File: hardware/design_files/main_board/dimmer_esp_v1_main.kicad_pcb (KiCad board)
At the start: 2 copper layers, 44 x 49.5 mm, 53 parts, among them IC1 PEC11S-929K-S0015, J1 SM05B-SRSS-TB_LF__SN_, J4 Conn_01x02, J5 Conn_01x02, J6 Conn_01x02, J7 Conn_01x04, J8 Screw_Terminal_01x03, K1 FTR-LYCA005Y, SW1 Commission, SW2 Reset, SW3 Toggle, U1 74AHC1G14, U2 LDO: SPX3819M5-L-3-3, U3 ESP32-C6-MINI, U4 SN74LV1T125DBVR, U6 SN74LVC1G74DCUR

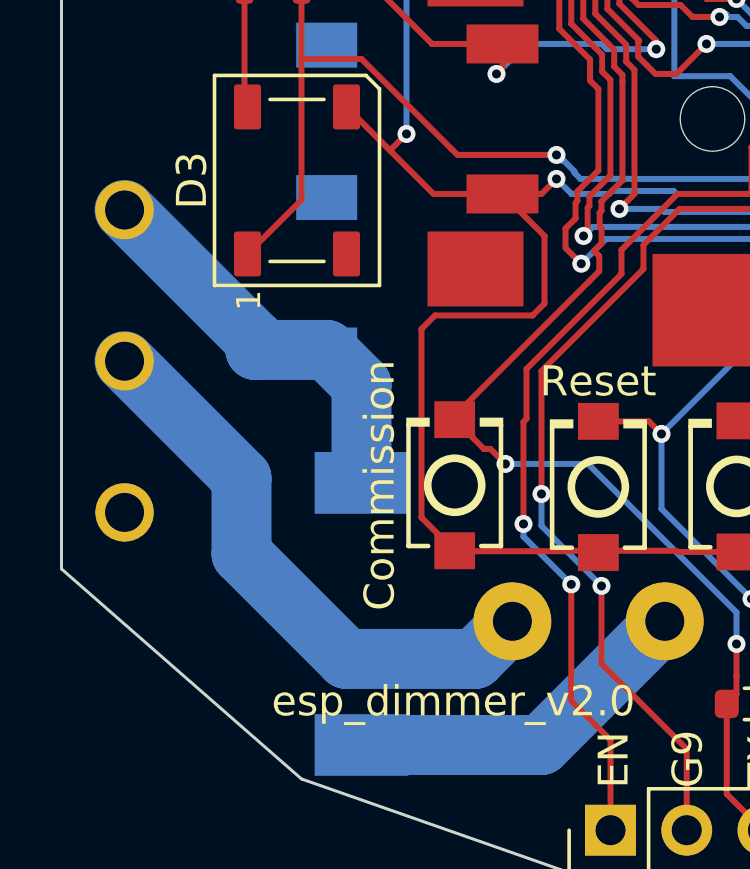
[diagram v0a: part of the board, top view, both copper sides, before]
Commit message: Fix trace before remove debug interface
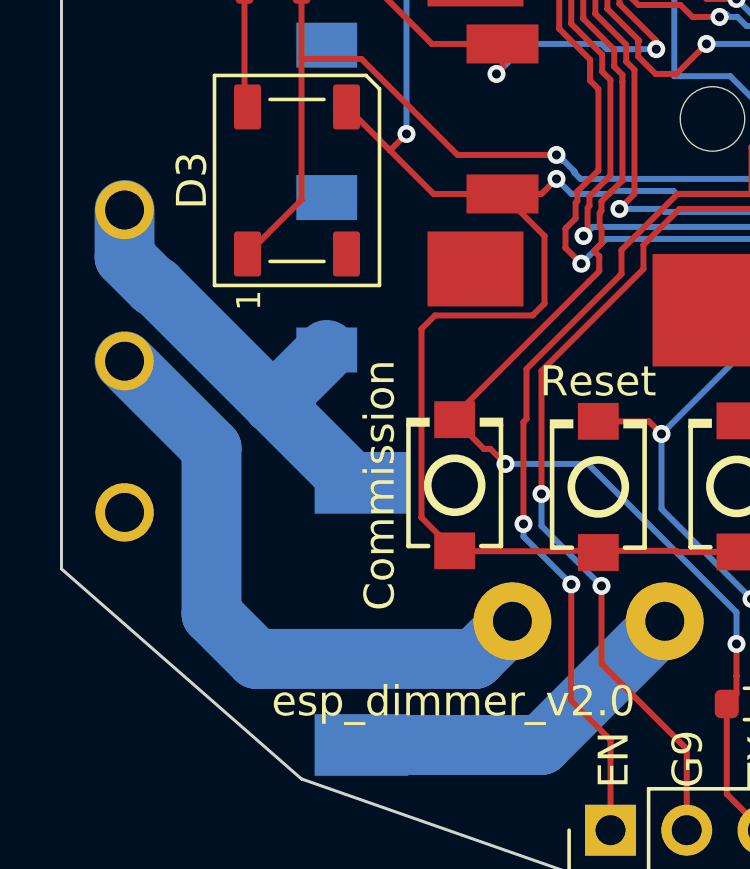
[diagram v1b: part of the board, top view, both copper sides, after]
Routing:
- net /HV4: track 19.0 -> 20.8 mm
- net /HV3: track 13.8 -> 15.1 mm
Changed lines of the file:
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@@
 	)
 	(segment
-		(start 151.963825 68.396612)
+		(start 152.552284 70.488123)
+		(end 148.638318 66.574157)
+		(width 2)
+		(layer "B.Cu")
+		(net 9)
+	)
+	(segment
+		(start 148.638318 66.574157)
+		(end 148.574157 66.574157)
+		(width 2)
+		(layer "B.Cu")
+		(net 9)
+	)
+	(segment
+		(start 147.60237 65.60237)
 		(end 147.60237 64.035157)
 		(width 2)
@@
 	)
 	(segment
-		(start 155.5 69.860763)
-		(end 154.339822 68.700585)
+		(start 154.339822 68.700585)
+		(end 152.552284 70.488123)
 		(width 2)
 		(layer "B.Cu")
@@
 	)
 	(segment
-		(start 155.5 73.1312)
-		(end 155.5 69.860763)
+		(start 155.195361 73.1312)
+		(end 152.552284 70.488123)
 		(width 2)
 		(layer "B.Cu")
@@
 	)
 	(segment
-		(start 151.963825 68.700585)
-		(end 151.963825 68.396612)
+		(start 155.5 73.1312)
+		(end 155.195361 73.1312)
 		(width 2)
 		(layer "B.Cu")
@@
 	)
 	(segment
-		(start 154.339822 68.700585)
-		(end 151.963825 68.700585)
+		(start 148.574157 66.574157)
+		(end 147.60237 65.60237)
 		(width 2)
 		(layer "B.Cu")
@@
 	)
 	(segment
-		(start 155 79)
-		(end 151.5 75.5)
+		(start 159.27526 79)
+		(end 152 79)
 		(width 2)
 		(layer "B.Cu")
@@
 	)
 	(segment
-		(start 151.5 72.972787)
-		(end 147.60237 69.075157)
+		(start 150.5 77.5)
+		(end 150.5 71.972787)
 		(width 2)
 		(layer "B.Cu")
@@
 	)
 	(segment
-		(start 151.5 75.5)
-		(end 151.5 72.972787)
+		(start 152 79)
+		(end 150.5 77.5)
 		(width 2)
 		(layer "B.Cu")
@@
 	)
 	(segment
-		(start 159.27526 79)
-		(end 155 79)
+		(start 160.529555 77.745705)
+		(end 159.27526 79)
 		(width 2)
 		(layer "B.Cu")
@@
 	)
 	(segment
-		(start 160.529555 77.745705)
-		(end 159.27526 79)
+		(start 150.5 71.972787)
+		(end 147.60237 69.075157)
 		(width 2)
 		(layer "B.Cu")

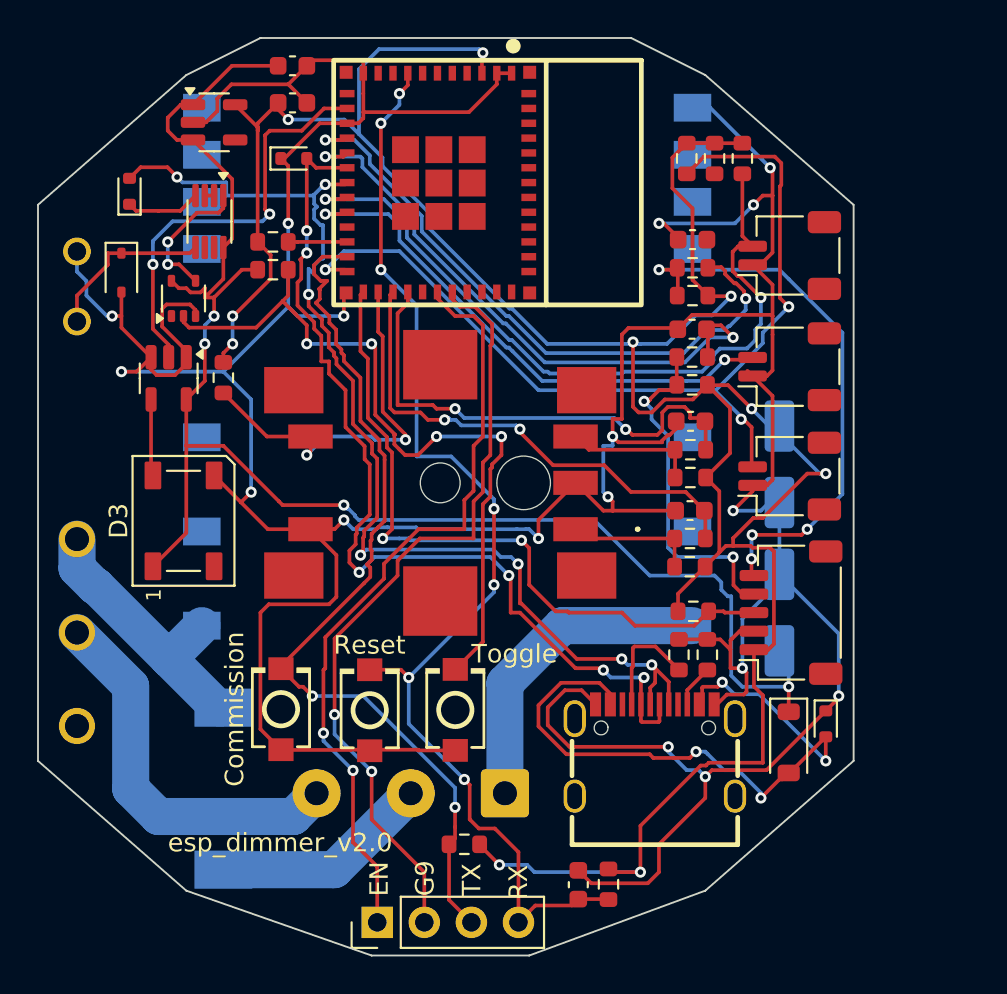
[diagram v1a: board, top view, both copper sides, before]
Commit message: Rework PCB, switch to bigger LDO, fix distance between high and low voltage
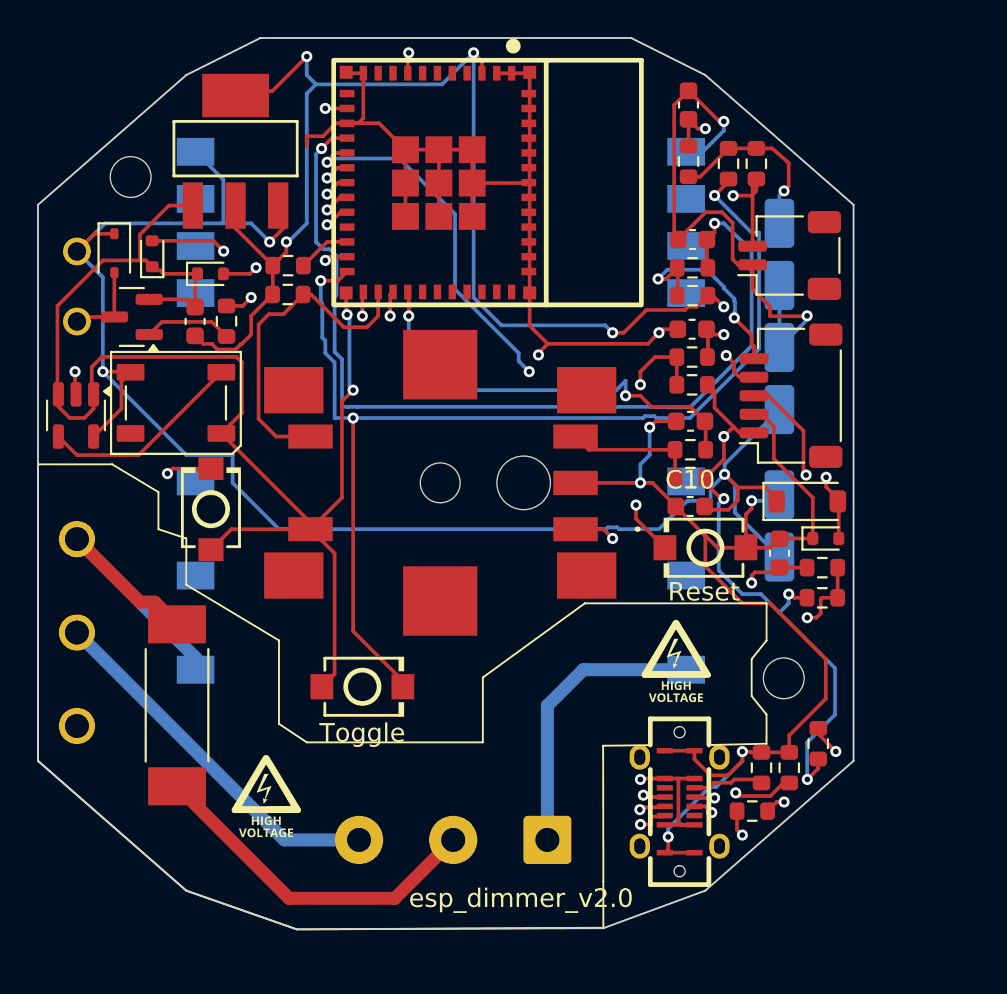
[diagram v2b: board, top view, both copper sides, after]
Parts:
- removed C6: 1u, Capacitor_SMD:C_0603_1608Metric
- removed J5, J6: Conn_01x02, Connector_JST:JST_SH_SM02B-SRSS-TB_1x02-1MP_P1.00mm_Horizontal
- removed J7: Conn_01x04, Connector_PinHeader_2.54mm:PinHeader_1x04_P2.54mm_Vertical
- removed R13: 10k, Resistor_SMD:R_0603_1608Metric
- removed U2: LDO: SPX3819M5-L-3-3, Package_TO_SOT_SMD:SOT-23-5
- removed U6: SN74LVC1G74DCUR, Package_SO:VSSOP-8_2.3x2mm_P0.5mm
- removed USB2: USB-TYPE-C-018, usb_jlc:USB-C_SMD-TYPE-C-31-M-12
- added C10: 0.1uF/50V(10%), Capacitor_SMD:C_0603_1608Metric, F.Cu at (180.7, 62.3)
- added C11: 10uF/25V(20%), Capacitor_SMD:C_Elec_4x5.4, B.Cu at (185.5, 63.3)
- added H1: MountingHole, MountingHole:MountingHole_2.2mm_M2_DIN965, F.Cu at (150.5, 44.5)
- added H2: MountingHole, MountingHole:MountingHole_2.2mm_M2_DIN965, F.Cu at (185.7, 71.5)
- added Q1: BC817, Package_TO_SOT_SMD:SOT-23, F.Cu at (150.6, 52.0)
- added U5: USB TYPE-C 16PLT-H10.0, usb_jlc:TYPE-C-SMD_USB4120-03-C, F.Cu at (180.1, 78.2)
- C3: value 47uF 16V ±20% -> 10uF/25V(20%)(NC); footprint Capacitor_SMD:C_Elec_5x5.4 -> Capacitor_SMD:C_Elec_4x5.4
- C4: value 47uF 16V ±20% -> 10uF/25V(20%); footprint Capacitor_SMD:C_Elec_5x5.4 -> Capacitor_SMD:C_Elec_4x5.4
- C7: value 1u -> 0.1uF/50V(10%)
- F1: moved to F.Cu
- R10: value 10k -> 1k
- U1: value 74AHC1G14 -> SGM2212-3.3XKC3G/TR; footprint Package_TO_SOT_SMD:SOT-353_SC-70-5 -> ldo_jlcpcb:SOT-223-3_L6.5-W3.4-P2.30-LS7.0-BR
- moved C5 42.5 mm to (180.6, 40.6)
- moved R14 39.2 mm to (180.6, 43.7), turned to 90 degrees
- moved R10 27.8 mm to (155.7, 52.3), turned to 90 degrees
- moved SW2 20.1 mm to (181.5, 64.5), turned to 180 degrees
- moved R8 19.9 mm to (187.6, 75.1), turned to 90 degrees
- moved D5 13.0 mm to (187.0, 62.0), turned to 0 degrees
- moved C7 12.9 mm to (154.0, 52.3), turned to -90 degrees
- moved C3 12.6 mm to (185.5, 55.4)
- moved J1 11.7 mm to (186.1, 56.3)
- moved SW1 11.4 mm to (154.8, 62.4)
- moved C4 11.3 mm to (185.5, 48.7)
- moved R19 11.2 mm to (184.0, 78.7), turned to 180 degrees
- moved D1 10.0 mm to (188.0, 64.0), turned to 0 degrees
- moved D2 9.21 mm to (151.7, 48.6), turned to 90 degrees
- moved R5 8.52 mm to (186.0, 76.4)
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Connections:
- D6 pad 1: Net-(D6-K) -> +5V
- D6 pad 2: GND -> Net-(D6-A)
- K1 pad 1: GND -> +5V
- K1 pad 2: Net-(D6-K) -> Net-(D6-A)
- R10 pad 1: +3.3V -> Net-(Q1-B)
- SW3 pad 2: Net-(R13-Pad2) -> /D18
- U1 pad 1: unconnected-(U1-NC-Pad1) -> GND
- U1 pad 2: Net-(R13-Pad2) -> +3.3V
- U1 pad 3: GND -> +5V
- U1 pad 4: Net-(U6-CLK) -> +3.3V
- U3 pad 36: unconnected-(U3-GND-Pad36) -> GND
- U3 pad 37: unconnected-(U3-GND-Pad37) -> GND
- U3 pad 38: unconnected-(U3-GND-Pad38) -> GND
- U3 pad 39: unconnected-(U3-GND-Pad39) -> GND
- U3 pad 40: unconnected-(U3-GND-Pad40) -> GND
- U3 pad 41: unconnected-(U3-GND-Pad41) -> GND
- U3 pad 42: unconnected-(U3-GND-Pad42) -> GND
- U3 pad 43: unconnected-(U3-GND-Pad43) -> GND
- U3 pad 44: unconnected-(U3-GND-Pad44) -> GND
- U3 pad 45: unconnected-(U3-GND-Pad45) -> GND
- U3 pad 46: unconnected-(U3-GND-Pad46) -> GND
- U3 pad 47: unconnected-(U3-GND-Pad47) -> GND
- U3 pad 48: unconnected-(U3-GND-Pad48) -> GND
- U3 pad 49: unconnected-(U3-GND-Pad49)_3 -> GND
- U3 pad 50: unconnected-(U3-GND-Pad50) -> GND
- U3 pad 52: unconnected-(U3-GND-Pad52) -> GND
- U3 pad 53: unconnected-(U3-GND-Pad53) -> GND
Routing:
- net /UART_TXD: track 42.6 -> 0.00 mm, vias 2 -> 0
- net /UART_RXD: track 41.8 -> 0.00 mm, vias 2 -> 0
- net Net-(R13-Pad2): track 40.5 -> 0.00 mm, vias 4 -> 0
- net /D19: track 37.8 -> 68.9 mm, vias 2 -> 3
- net /D12: track 51.4 -> 80.5 mm, vias 6 -> 4
- net /D09: track 48.5 -> 70.5 mm, vias 2 -> 3
- net /D15: track 28.9 -> 8.60 mm
- net Net-(J1-Pad5): track 30.9 -> 11.5 mm, vias 4 -> 2
- net +3.3V: track 150.6 -> 131.5 mm, vias 10 -> 11
- net /D06: track 33.8 -> 50.3 mm
- net /D13: track 60.8 -> 73.4 mm, vias 7 -> 4
- net Net-(IC1-CCW): track 7.08 -> 18.6 mm, vias 0 -> 2
- net /D18: track 50.5 -> 60.5 mm
- net Net-(D6-K): track 9.24 -> 0.00 mm
- net Net-(U6-CLK): track 7.51 -> 0.00 mm, vias 2 -> 0
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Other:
- board size 44 x 49.5 mm -> 44 x 48.1 mm
- copper layers 2 -> 4
- board text removed: "EN"
- board text removed: "G9"
- board text removed: "RX"
- board text removed: "TX"

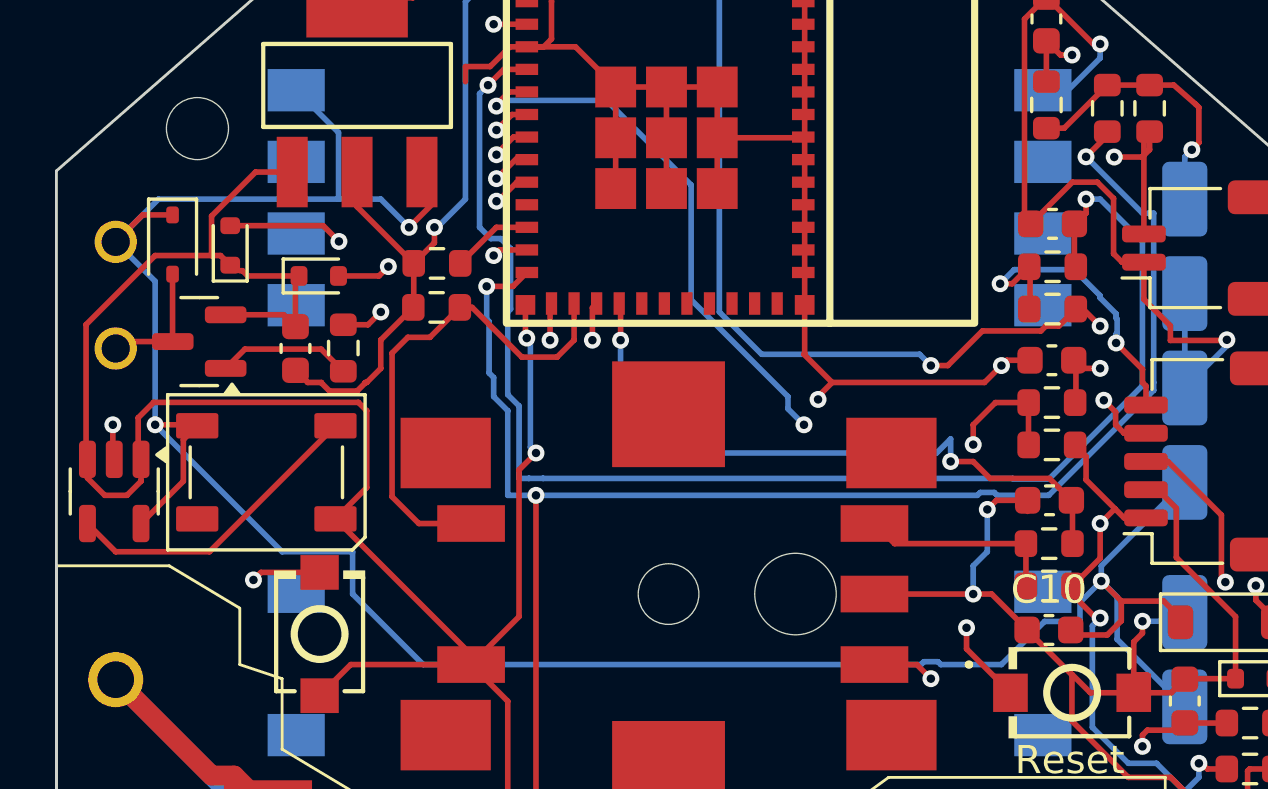
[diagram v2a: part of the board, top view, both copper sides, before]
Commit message: Hardware: Add pull-down to GPIO15 to ensure JTAG via USB works
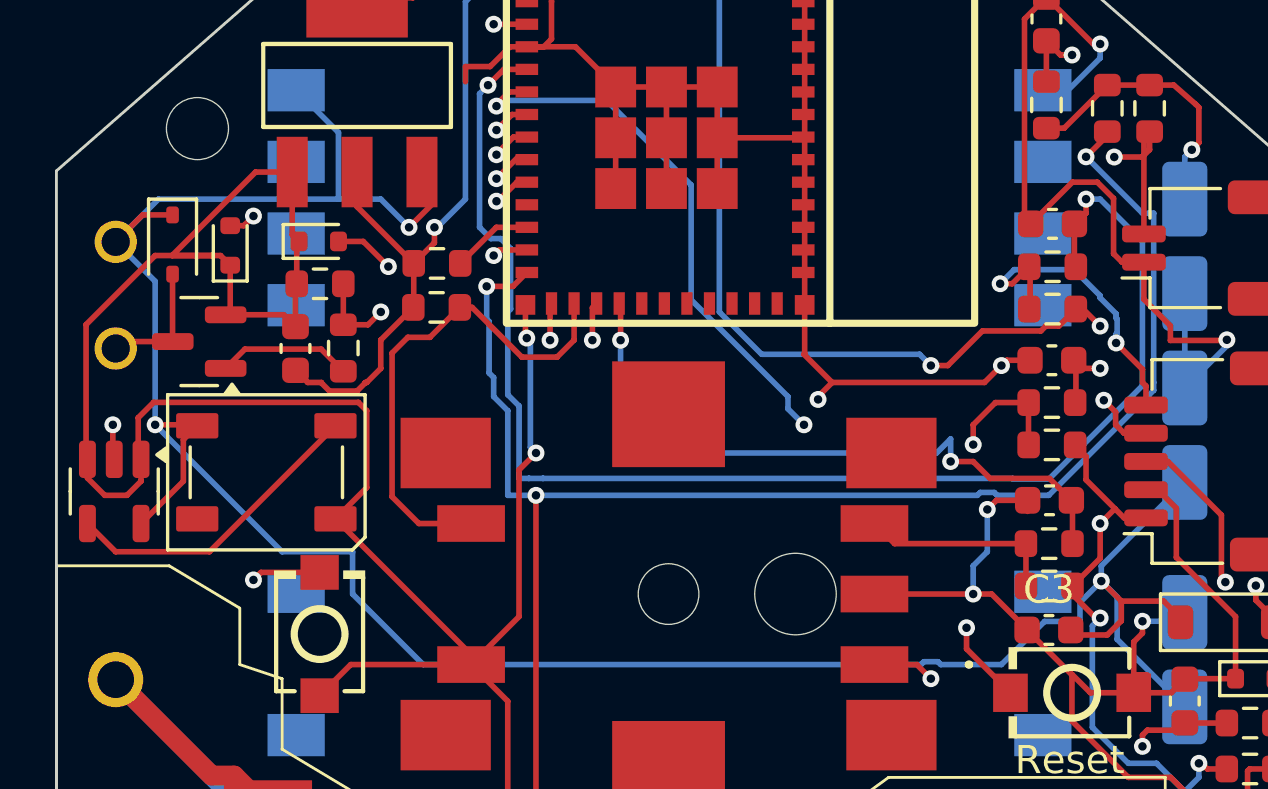
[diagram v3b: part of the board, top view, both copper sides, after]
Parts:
- added R6: 10k, Resistor_SMD:R_0603_1608Metric, F.Cu at (154.8, 50.0)
- moved D5 1.22 mm to (154.8, 48.5)
- renumbered C9 to C10, C10 to C3, C11 to C4, C7 to C5, C4 to C6, C5 to C7, C3 to C8, C8 to C9, D6 to D1, D1 to D2, D2 to D3, D5 to D4, D4 to D5, D3 to D6, J8 to J1, J1 to J2, J4 to J3, PS2 to PS1, R2 to R1, R6 to R10, R5 to R11, R14 to R12, R15 to R13, R16 to R14, R17 to R15, R18 to R16, R12 to R17, R19 to R18, R9 to R19, R1 to R2, R7 to R5, R10 to R7, R11 to R8, R8 to R9, SW3 to SW2, SW2 to SW3, U5 to U2, U4 to U3, U3 to U4
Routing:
- net GND: track 260.9 -> 266.3 mm
- net /D01: track 24.1 -> 27.4 mm
- net /D15: track 8.60 -> 10.1 mm

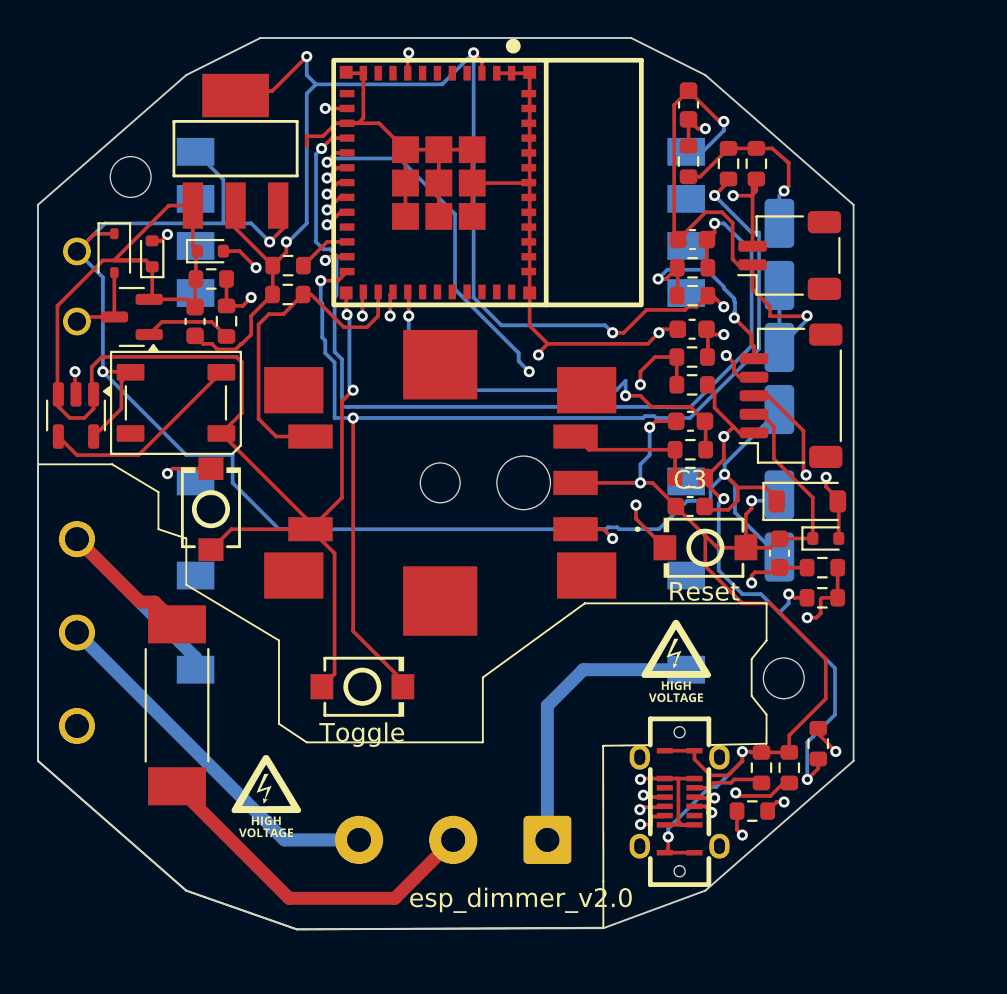
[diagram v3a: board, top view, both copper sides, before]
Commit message: Add changes to PCB layout
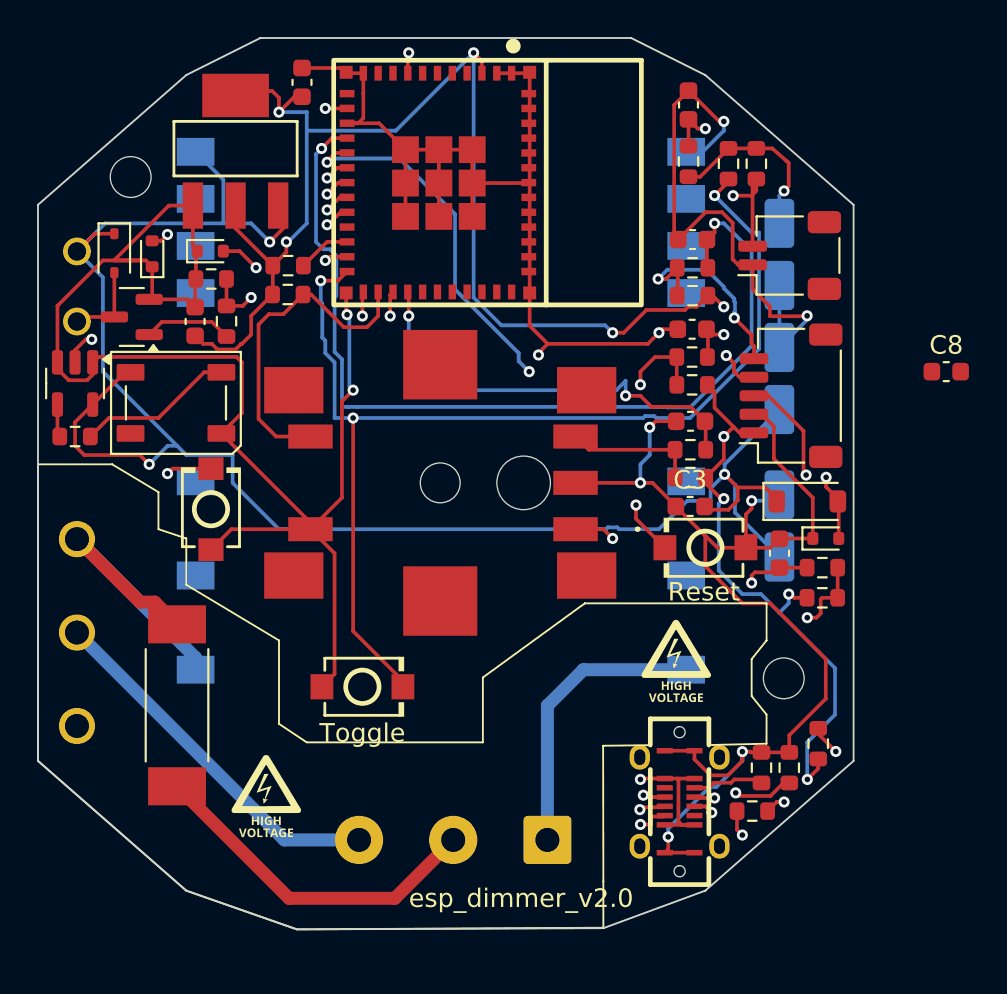
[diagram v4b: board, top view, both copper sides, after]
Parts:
- added C10: 0.1uF, Capacitor_SMD:C_0603_1608Metric, F.Cu at (159.7, 39.4)
- added C8: 0.1uF, Capacitor_SMD:C_0603_1608Metric, F.Cu at (194.5, 55.0)
- added R20: 330, Resistor_SMD:R_0603_1608Metric, F.Cu at (147.5, 58.5)
- C9: renamed from C8; value 10uF/25V(20%)(NC) -> 10uF/25V(20%)
- moved U3 1.73 mm to (147.5, 55.6)
- renumbered C9 to C11, C10 to C12
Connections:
- U3 pad 4: Net-(D6-DIN) -> Net-(U3-Y)
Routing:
- net +5V: track 90.2 -> 96.1 mm
- net GND: track 266.3 -> 261.9 mm
- net /D01: track 27.4 -> 24.8 mm
- net Net-(D6-DIN): track 11.1 -> 8.50 mm
- net Net-(U3-Y): track 0.00 -> 2.44 mm
